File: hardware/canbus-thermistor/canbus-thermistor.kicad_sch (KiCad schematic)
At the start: 33 parts, among them J1 USB_B_Micro, J2 UART, J3 NTC Thermistor, J4 CANBus, J5 CANBus, J6 SWD, Q1 2N7002, Q2 2N7002, U1 MCP1754S-3302xCB, U2 STM32F042F6Px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

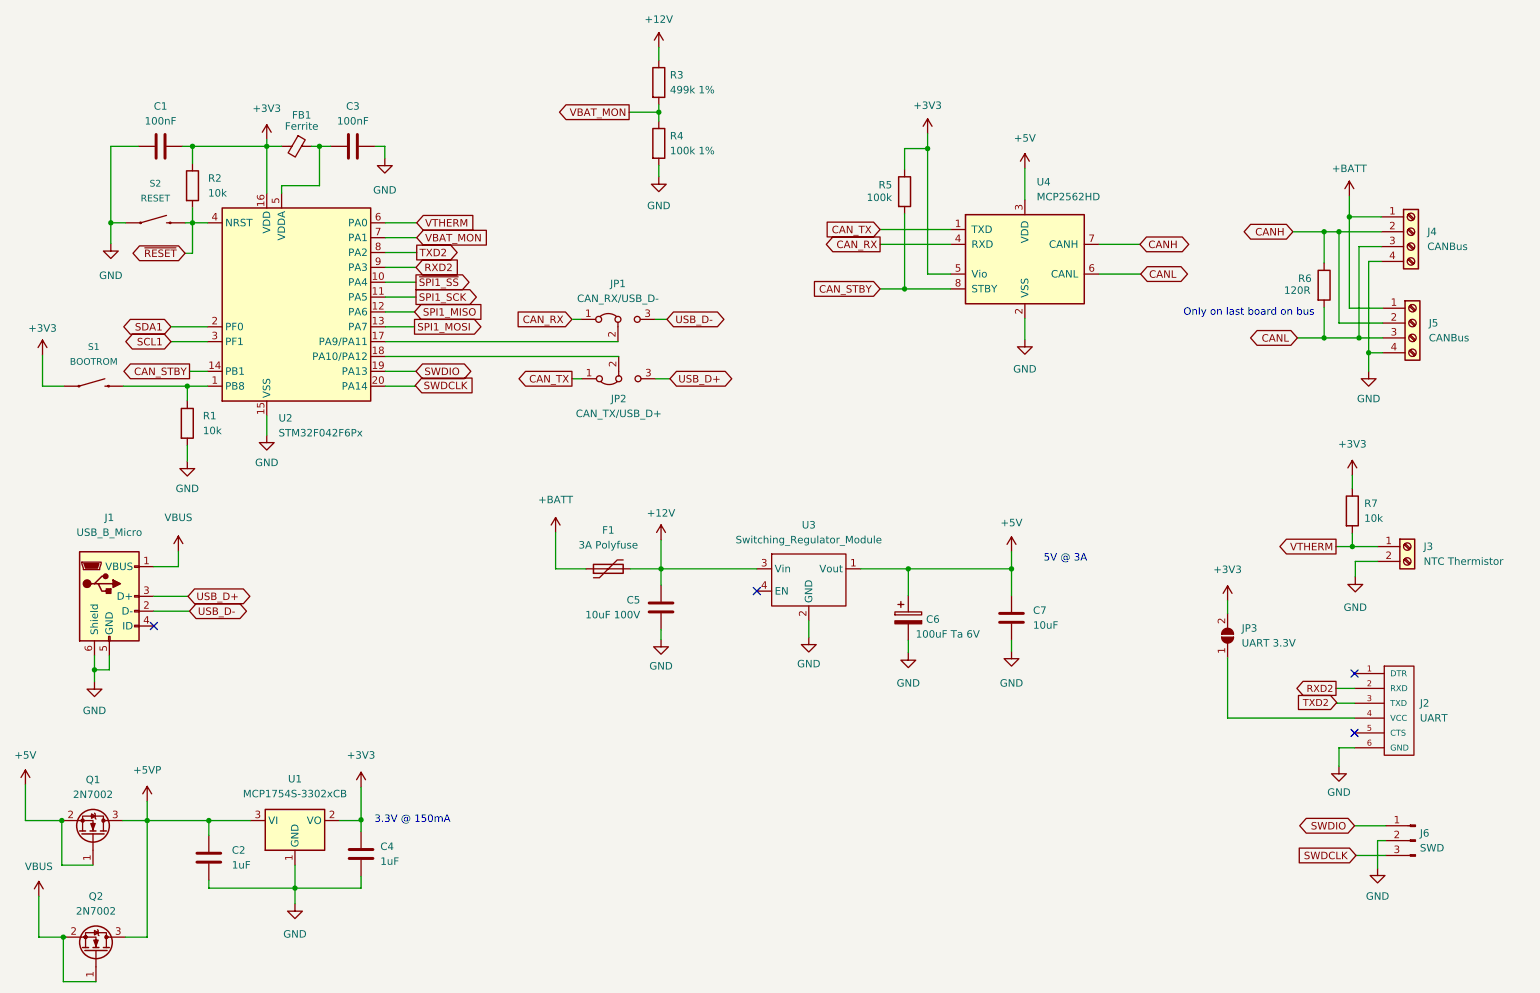
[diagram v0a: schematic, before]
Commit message: Add CANBus Thermistor layout
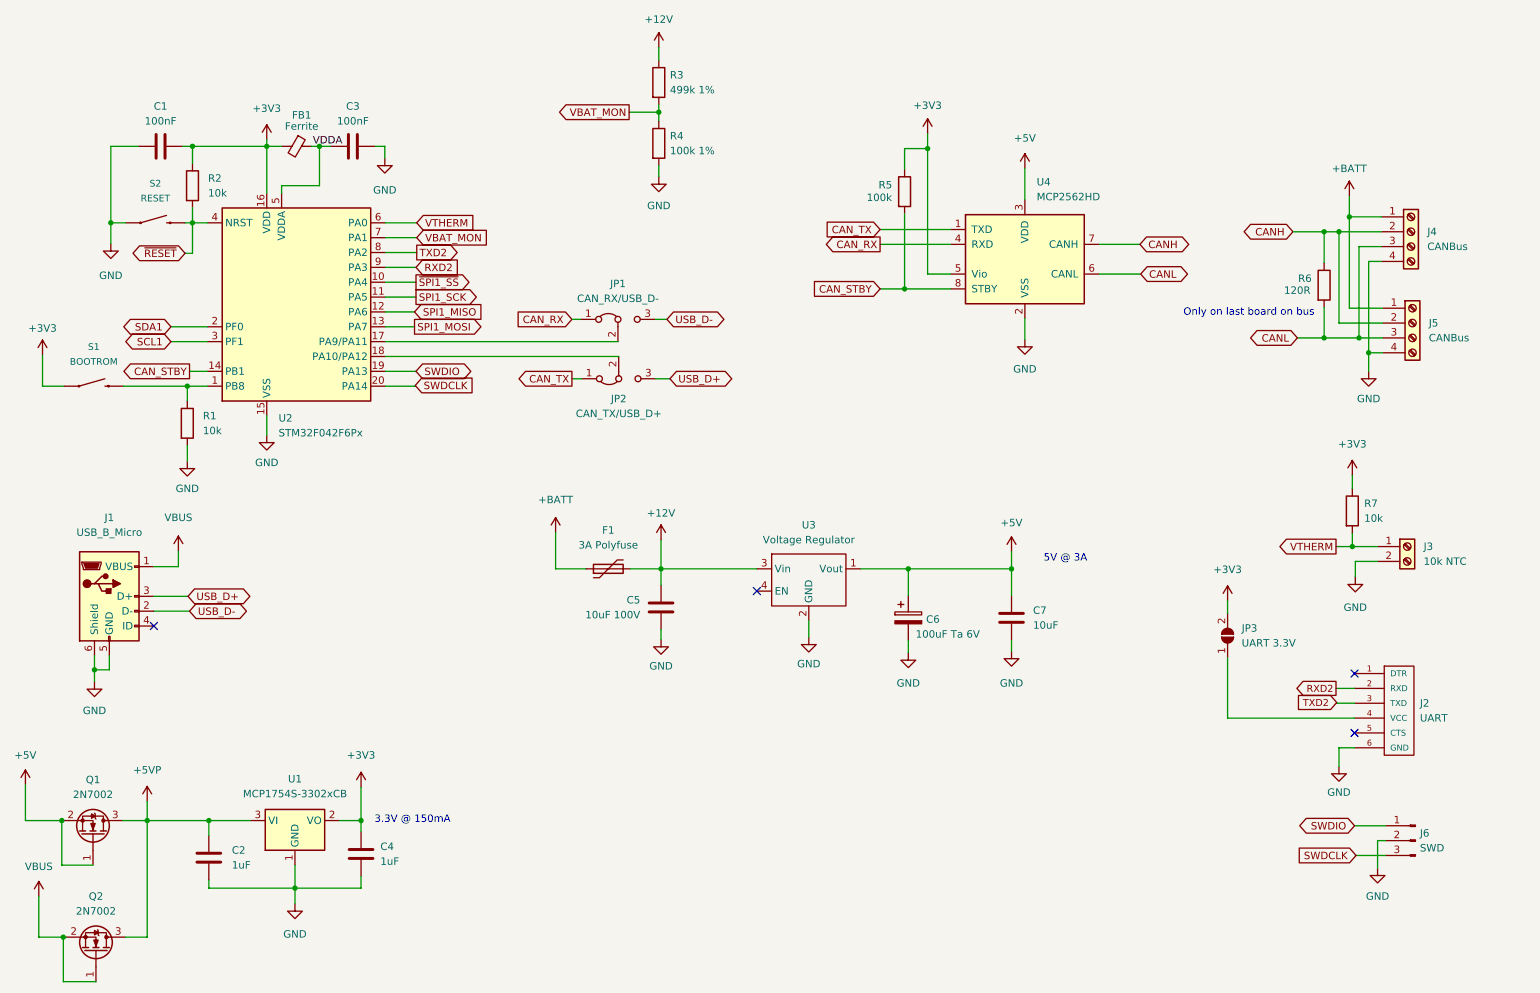
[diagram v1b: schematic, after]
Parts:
- J3: value NTC Thermistor -> 10k NTC
- S1, S2: symbol SparkFun-Switches:MOMENTARY-SWITCH-SPST-PTH-6.0MM -> Beirdo:MOMENTARY-SWITCH-SPST-PTH-6.0MM
- U3: value Switching_Regulator_Module -> Voltage Regulator
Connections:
- net +3V3: now also C4.1, U1.2 (VO)
- net VDDA: now reaches C3.1, FB1.1, U2.5 (VDDA)
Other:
- company: (none) -> Gavin Hurlbut
- title: (none) -> CANBus Thermistor Sensor
